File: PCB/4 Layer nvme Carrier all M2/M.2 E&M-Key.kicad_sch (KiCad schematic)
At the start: 23 parts, among them J200 Bus_M.2_Socket_M, J300 Bus_M.2_Socket_E

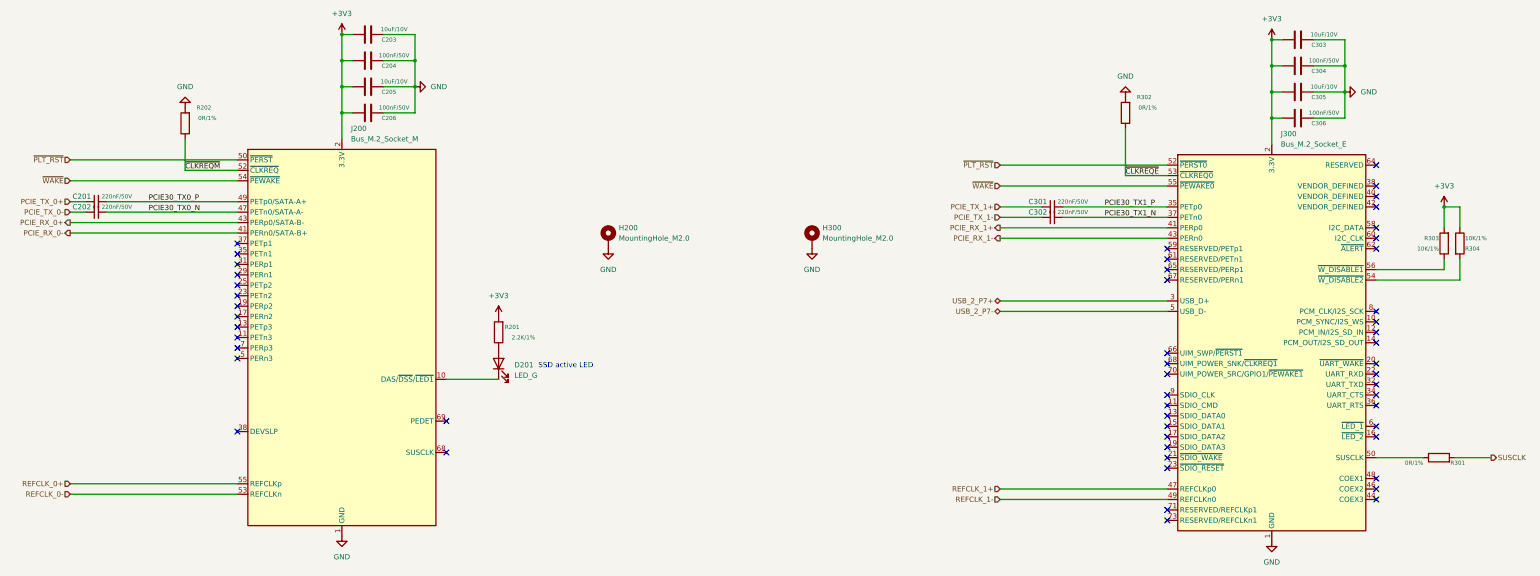
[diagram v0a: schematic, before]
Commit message: first all-M.2 version
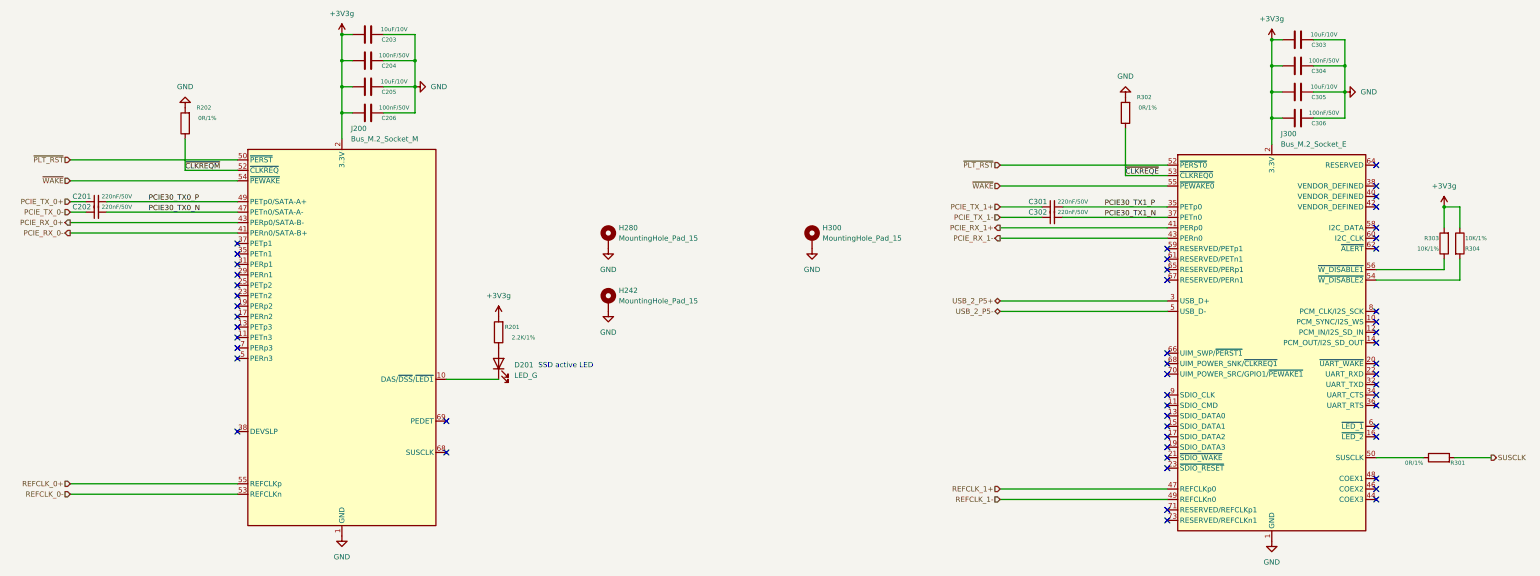
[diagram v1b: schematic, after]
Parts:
- added H242: MountingHole_Pad_15, A_HDJ_Library:MountingHole_3mm_M2_Pad_TopOnly, symbol Mechanical:MountingHole_Pad
- H280: renamed from H200; value MountingHole_M2.0 -> MountingHole_Pad_15; footprint A_HDJ_Library:MountingHole_2.75mm_M2_4.4mm_Pad_TopOnly -> A_HDJ_Library:MountingHole_3mm_M2_Pad_TopOnly; LCSC Part # (none) -> C5221852; MPN (none) -> SMTWEM215STR; Package (none) -> MountingHole
- H300: value MountingHole_M2.0 -> MountingHole_Pad_15; footprint A_HDJ_Library:MountingHole_2.75mm_M2_4.4mm_Pad_TopOnly -> A_HDJ_Library:MountingHole_3mm_M2_Pad_TopOnly; LCSC Part # (none) -> C5221852; MPN (none) -> SMTWEM215STR; Package (none) -> MountingHole
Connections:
- net GND: now also H242.1
- net +3V3 renamed +3V3g
- net USB_2_P7+ renamed USB_2_P5+
- net USB_2_P7- renamed USB_2_P5-
